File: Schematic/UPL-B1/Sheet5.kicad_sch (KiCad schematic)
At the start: 102 parts, among them P53 TestPoint, P54 TestPoint, P55 TestPoint, P56 TestPoint, P57 TestPoint, P58 TestPoint, X50 Conn_01x03_Pin_Bridge, X51 Conn_01x03_Pin_Bridge, X52 Conn_01x03_Pin_Bridge

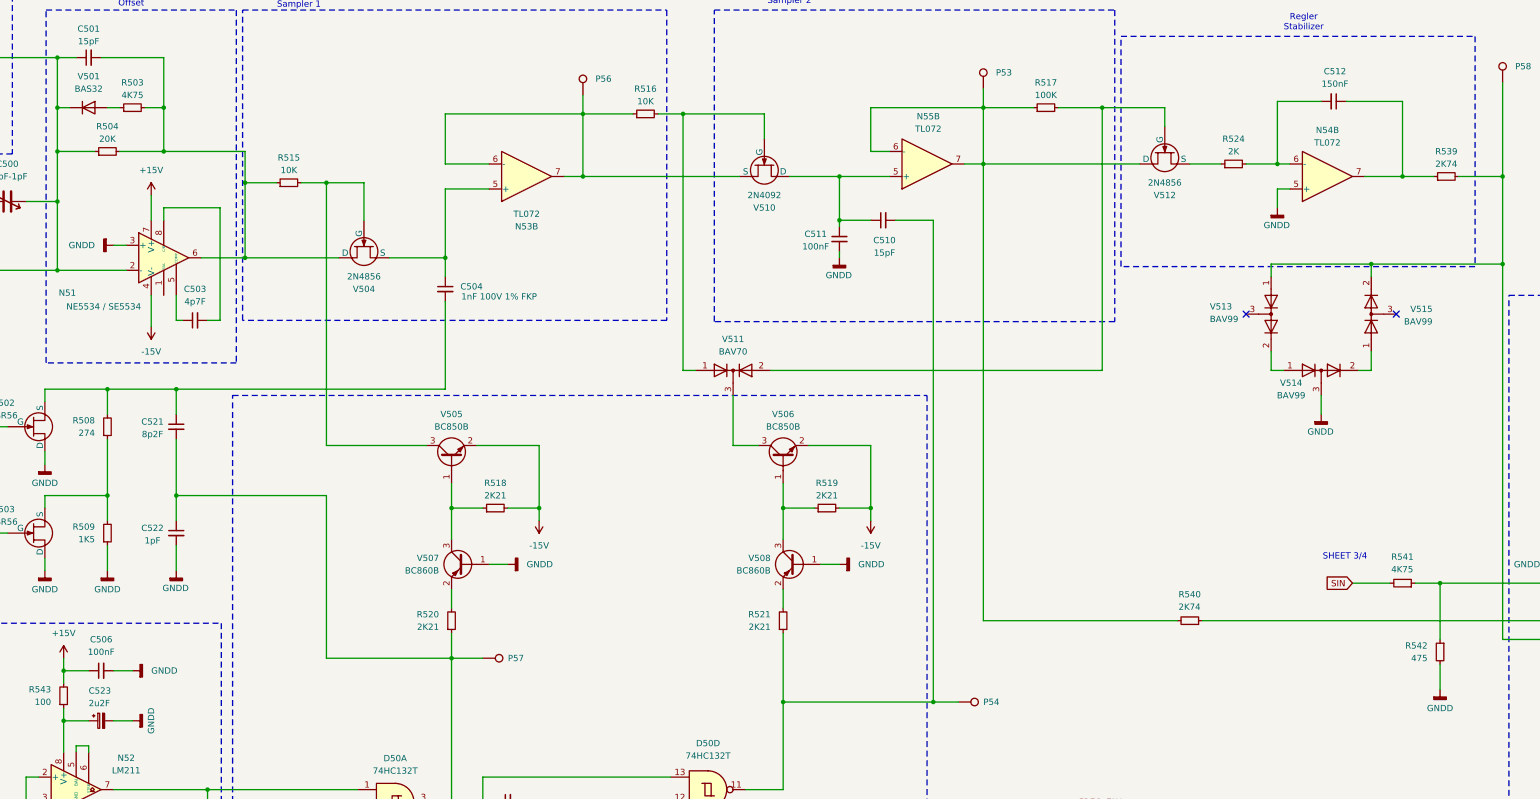
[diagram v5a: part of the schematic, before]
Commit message: added majority of footprints
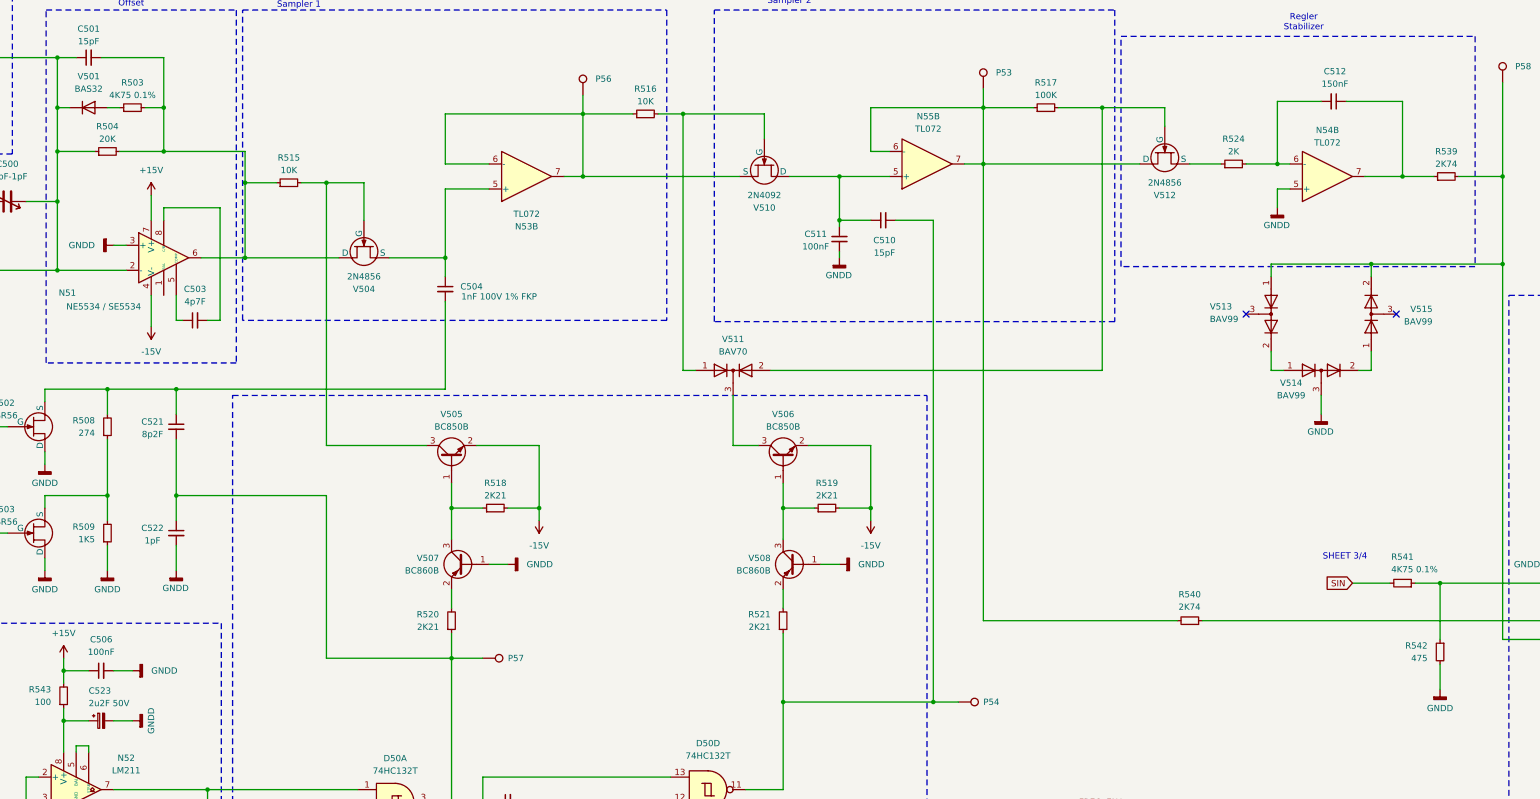
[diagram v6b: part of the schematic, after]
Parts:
- C501, C502, C503, C505, C506, C507, C509, C510, C511, C515, C516, C517, C518, C520, C521, C522: footprint (none) -> Capacitor_SMD:C_1206_3216Metric_Pad1.33x1.80mm_HandSolder
- C508, C519: footprint (none) -> Capacitor_THT:C_Radial_D6.3mm_H11.0mm_P2.50mm
- C523: value 2u2F -> 2u2F 50V; footprint (none) -> Capacitor_THT:C_Radial_D6.3mm_H11.0mm_P2.50mm
- D50: footprint (none) -> Package_SO:SOIC-14_3.9x8.7mm_P1.27mm
- N50, N51, N52, N53, N54, N55, N56: footprint (none) -> Package_SO:SOIC-8_3.9x4.9mm_P1.27mm
- P53, P54, P55, P56, P57, P58: footprint (none) -> Connector_PinHeader_1.00mm:PinHeader_1x01_P1.00mm_Vertical
- R500, R501, R504, R506, R507, R508, R509, R510, R511, R512, R513, R514, R515, R516, R517, R518, R519, R520, R521, R522, R523, R524, R525, R526, R527, R528, R529, R530, R531, R532, R533, R534, R535, R536, R537, R538, R539, R540, R542, R543: footprint (none) -> Resistor_SMD:R_1206_3216Metric_Pad1.30x1.75mm_HandSolder
- R502: footprint (none) -> Resistor_THT:R_Axial_DIN0204_L3.6mm_D1.6mm_P7.62mm_Horizontal
- R503, R541: value 4K75 -> 4K75 0.1%; footprint (none) -> R_Axial_DIN0204_L3.6mm_D1.6mm_P7.62mm_Horizontal
- R505: footprint (none) -> R_Axial_DIN0204_L3.6mm_D1.6mm_P7.62mm_Horizontal
- V500: footprint (none) -> Diode_THT:D_DO-35_SOD27_P7.62mm_Horizontal
- V502, V503: footprint (none) -> Package_TO_SOT_SMD:SOT-23
- V504, V510, V512: footprint (none) -> Package_TO_SOT_THT:TO-52-3
- V516: footprint (none) -> Diode_THT:D_DO-41_SOD81_P10.16mm_Horizontal

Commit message: Rough component outline on PCB
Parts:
- R503, R541: footprint R_Axial_DIN0204_L3.6mm_D1.6mm_P7.62mm_Horizontal -> Resistor_SMD:R_1206_3216Metric_Pad1.30x1.75mm_HandSolder
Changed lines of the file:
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@@
 			)
 		)
-		(property "Footprint" "R_Axial_DIN0204_L3.6mm_D1.6mm_P7.62mm_Horizontal"
+		(property "Footprint" "Resistor_SMD:R_1206_3216Metric_Pad1.30x1.75mm_HandSolder"
 			(at 127 129.54 0)
 			(effects
@@
 			)
 		)
-		(property "Footprint" "R_Axial_DIN0204_L3.6mm_D1.6mm_P7.62mm_Horizontal"
+		(property "Footprint" "Resistor_SMD:R_1206_3216Metric_Pad1.30x1.75mm_HandSolder"
 			(at 384.81 226.06 0)
 			(effects

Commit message: ERC fixes.
- Power flags added for power nets "hanging" off resistors.
- Add missing NC-markers for intentionally unconnected parts
- Fix -15V bridge between circuits on S4/S3
- Add +5 to /CLR of DAC
- Use non-hierachical labels on main sheet.
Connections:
- no-connect marks 2 -> 3
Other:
- note added: "Hmm. Looks like the bodge is documented dodgey.."
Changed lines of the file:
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@@
 		)
 	)
+	(text "Hmm. Looks like the bodge is documented dodgey.."
+		(exclude_from_sim no)
+		(at 167.386 284.226 90)
+		(effects
+			(font
+				(size 1.27 1.27)
+			)
+		)
+	)
 	(text "SHEET 3/4"
 		(exclude_from_sim no)
@@
 	)
 	(junction
+		(at 453.39 199.39)
+		(diameter 0)
+		(color 0 0 0 0)
+	)
+	(junction
 		(at 149.86 144.78)
 		(diameter 0)
@@
 	)
 	(junction
+		(at 170.18 300.99)
+		(diameter 0)
+		(color 0 0 0 0)
+	)
+	(junction
 		(at 111.76 138.43)
 		(diameter 0)
@@
 	)
 	(no_connect
+		(at 133.35 167.64)
+	)
+	(no_connect
 		(at 383.54 171.45)
 	)
@@
 	(wire
 		(pts
+			(xy 453.39 199.39) (xy 453.39 208.28)
+		)
+		(stroke
+			(width 0)
+			(type default)
+		)
+	)
+	(wire
+		(pts
 			(xy 510.54 232.41) (xy 514.35 232.41)
 		)
@@
 	(wire
 		(pts
+			(xy 170.18 300.99) (xy 170.18 304.8)
+		)
+		(stroke
+			(width 0)
+			(type default)
+		)
+	)
+	(wire
+		(pts
 			(xy 123.19 254) (xy 127 254)
 		)
@@
 	(wire
 		(pts
-			(xy 453.39 195.58) (xy 453.39 208.28)
+			(xy 453.39 195.58) (xy 453.39 199.39)
 		)
 		(stroke
@@
 	(wire
 		(pts
-			(xy 170.18 290.83) (xy 170.18 304.8)
+			(xy 170.18 290.83) (xy 170.18 300.99)
 		)
 		(stroke
@@
 	)
 	(symbol
+		(lib_id "power:PWR_FLAG")
+		(at 113.03 254 90)
+		(unit 1)
+		(exclude_from_sim no)
+		(in_bom yes)
+		(on_board yes)
+		(dnp no)
+		(fields_autoplaced yes)
+		(property "Reference" "#FLG08"
+			(at 111.125 254 0)
+			(effects
+				(font
+					(size 1.27 1.27)
+				)
+				(hide yes)
+			)
+		)
+		(property "Value" "PWR_FLAG"
+			(at 109.22 253.9999 90)
+			(effects
+				(font
+					(size 1.27 1.27)
+				)
+				(justify left)
+			)
+		)
+		(property "Footprint" ""
+			(at 113.03 254 0)
+			(effects
+				(font
+					(size 1.27 1.27)
+				)
+				(hide yes)
+			)
+		)
+		(property "Datasheet" "~"
+			(at 113.03 254 0)
+			(effects
+				(font
+					(size 1.27 1.27)
+				)
+				(hide yes)
+			)
+		)
+		(property "Description" "Special symbol for telling ERC where power comes from"
+			(at 113.03 254 0)
+			(effects
+				(font
+					(size 1.27 1.27)
+				)
+				(hide yes)
+			)
+		)
+		(pin "1"
+		)
+		(instances
+			(project ""
+				(path "/812de09b-8b67-463d-bf96-bb3aeeb1ed8d/6f377b57-c1d4-477b-840b-189645bd7d4e"
+					(reference "#FLG08")
+					(unit 1)
+				)
+			)
+		)
+	)
+	(symbol
 		(lib_id "power:+5V")
 		(at 276.86 213.36 180)
@@
 	)
 	(symbol
+		(lib_id "power:PWR_FLAG")
+		(at 170.18 300.99 270)
+		(unit 1)
+		(exclude_from_sim no)
+		(in_bom yes)
+		(on_board yes)
+		(dnp no)
+		(fields_autoplaced yes)
+		(property "Reference" "#FLG09"
+			(at 172.085 300.99 0)
+			(effects
+				(font
+					(size 1.27 1.27)
+				)
+				(hide yes)
+			)
+		)
+		(property "Value" "PWR_FLAG"
+			(at 173.99 300.9899 90)
+			(effects
+				(font
+					(size 1.27 1.27)
+				)
+				(justify left)
+			)
+		)
+		(property "Footprint" ""
+			(at 170.18 300.99 0)
+			(effects
+				(font
+					(size 1.27 1.27)
+				)
+				(hide yes)
+			)
+		)
+		(property "Datasheet" "~"
+			(at 170.18 300.99 0)
+			(effects
+				(font
+					(size 1.27 1.27)
+				)
+				(hide yes)
+			)
+		)
+		(property "Description" "Special symbol for telling ERC where power comes from"
+			(at 170.18 300.99 0)
+			(effects
+				(font
+					(size 1.27 1.27)
+				)
+				(hide yes)
+			)
+		)
+		(pin "1"
+		)
+		(instances
+			(project ""
+				(path "/812de09b-8b67-463d-bf96-bb3aeeb1ed8d/6f377b57-c1d4-477b-840b-189645bd7d4e"
+					(reference "#FLG09")
+					(unit 1)
+				)
+			)
+		)
+	)
+	(symbol
 		(lib_id "Device:R_Small")
 		(at 500.38 227.33 90)
@@
 					(unit 1)
 				)
+			)
+		)
+	)
+	(symbol
+		(lib_id "power:PWR_FLAG")
+		(at 453.39 199.39 270)
+		(unit 1)
+		(exclude_from_sim no)
+		(in_bom yes)
+		(on_board yes)
+		(dnp no)
+		(fields_autoplaced yes)
+		(property "Reference" "#FLG010"
+			(at 455.295 199.39 0)
+			(effects
+				(font
+					(size 1.27 1.27)
+				)
+				(hide yes)
+			)
+		)
+		(property "Value" "PWR_FLAG"
+			(at 457.2 199.3899 90)
+			(effects
+				(font
+					(size 1.27 1.27)
+				)
+				(justify left)
+			)
+		)
+		(property "Footprint" ""
+			(at 453.39 199.39 0)
+			(effects
+				(font
+					(size 1.27 1.27)
+				)
+				(hide yes)
+			)
+		)
+		(property "Datasheet" "~"
+			(at 453.39 199.39 0)
+			(effects
+				(font
+					(size 1.27 1.27)
+				)
+				(hide yes)
+			)
+		)
+		(property "Description" "Special symbol for telling ERC where power comes from"
+			(at 453.39 199.39 0)
+			(effects
+				(font
+					(size 1.27 1.27)
+				)
+				(hide yes)
+			)
+		)
+		(pin "1"
+		)
+		(instances
+			(project ""
+				(path "/812de09b-8b67-463d-bf96-bb3aeeb1ed8d/6f377b57-c1d4-477b-840b-189645bd7d4e"
+					(reference "#FLG010")
+					(unit 1)
+				)
